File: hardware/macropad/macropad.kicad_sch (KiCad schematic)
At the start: 32 parts, among them J1 SWD, J2 USB_C_Receptacle, J4 display(4x1), SW1 SW_Push, SW10 SW_SPDT, SW11 SW_Push, SW12 Enc1, SW13 Enc2, SW2 SW_Push, SW3 SW_Push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

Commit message: updated footprints
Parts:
- C1, C3: footprint (none) -> Capacitor_SMD:C_0805_2012Metric
- C17, C18: footprint Capacitor_SMD:C_0805_2012Metric -> Capacitor_SMD:C_0603_1608Metric
- C2, C4, C5, C6, C8, C9: footprint (none) -> Capacitor_SMD:C_0603_1608Metric
- R1, R2, R4: footprint (none) -> Resistor_SMD:R_0603_1608Metric
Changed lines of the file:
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@@
 			)
 		)
-		(property "Footprint" ""
+		(property "Footprint" "Capacitor_SMD:C_0603_1608Metric"
 			(at 82.2452 46.99 0)
 			(effects
@@
 			)
 		)
-		(property "Footprint" ""
+		(property "Footprint" "Capacitor_SMD:C_0805_2012Metric"
 			(at 61.9252 46.99 0)
 			(effects
@@
 			)
 		)
-		(property "Footprint" ""
+		(property "Footprint" "Resistor_SMD:R_0603_1608Metric"
 			(at 223.012 68.58 90)
 			(effects
@@
 			)
 		)
-		(property "Footprint" ""
+		(property "Footprint" "Capacitor_SMD:C_0603_1608Metric"
 			(at 72.0852 46.99 0)
 			(effects
@@
 			)
 		)
-		(property "Footprint" "Capacitor_SMD:C_0805_2012Metric"
+		(property "Footprint" "Capacitor_SMD:C_0603_1608Metric"
 			(at 88.5952 142.24 0)
 			(effects
@@
 			)
 		)
-		(property "Footprint" ""
+		(property "Footprint" "Capacitor_SMD:C_0603_1608Metric"
 			(at 112.7252 46.99 0)
 			(effects
@@
 			)
 		)
-		(property "Footprint" ""
+		(property "Footprint" "Capacitor_SMD:C_0603_1608Metric"
 			(at 102.5652 46.99 0)
 			(effects
@@
 			)
 		)
-		(property "Footprint" "Capacitor_SMD:C_0805_2012Metric"
+		(property "Footprint" "Capacitor_SMD:C_0603_1608Metric"
 			(at 113.9952 142.24 0)
 			(effects
@@
 			)
 		)
-		(property "Footprint" ""
+		(property "Footprint" "Capacitor_SMD:C_0805_2012Metric"
 			(at 322.2752 73.66 0)
 			(effects
@@
 			)
 		)
-		(property "Footprint" ""
+		(property "Footprint" "Resistor_SMD:R_0603_1608Metric"
 			(at 391.668 156.21 90)
 			(effects
@@
 			)
 		)
-		(property "Footprint" ""
+		(property "Footprint" "Capacitor_SMD:C_0603_1608Metric"
 			(at 92.4052 46.99 0)
 			(effects
@@
 			)
 		)
-		(property "Footprint" ""
+		(property "Footprint" "Capacitor_SMD:C_0603_1608Metric"
 			(at 113.03 89.8652 0)
 			(effects
@@
 			)
 		)
-		(property "Footprint" ""
+		(property "Footprint" "Resistor_SMD:R_0603_1608Metric"
 			(at 400.558 153.67 90)
 			(effects

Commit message: updated footprints
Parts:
- SW11: footprint (none) -> Button_Switch_SMD:SW_Push_1P1T_NO_E-Switch_TL3301NxxxxxG
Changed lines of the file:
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@@
 			)
 		)
-		(property "Footprint" ""
+		(property "Footprint" "Button_Switch_SMD:SW_Push_1P1T_NO_E-Switch_TL3301NxxxxxG"
 			(at 116.84 74.93 0)
 			(effects

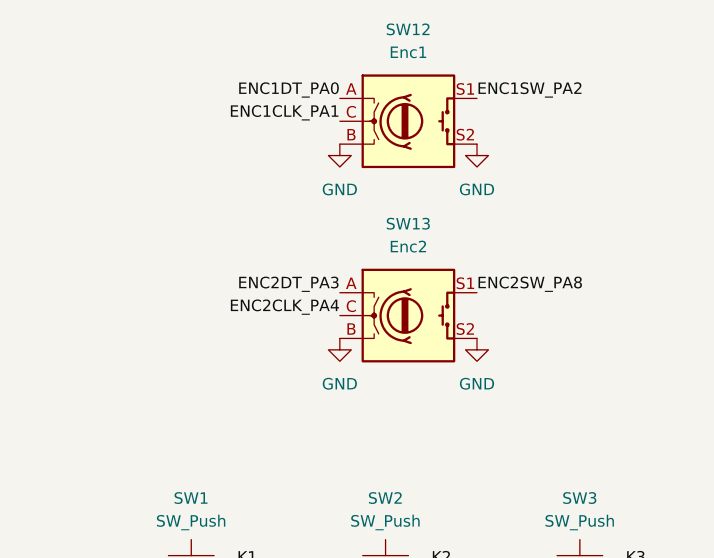
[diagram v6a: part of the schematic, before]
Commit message: replaced enc with module
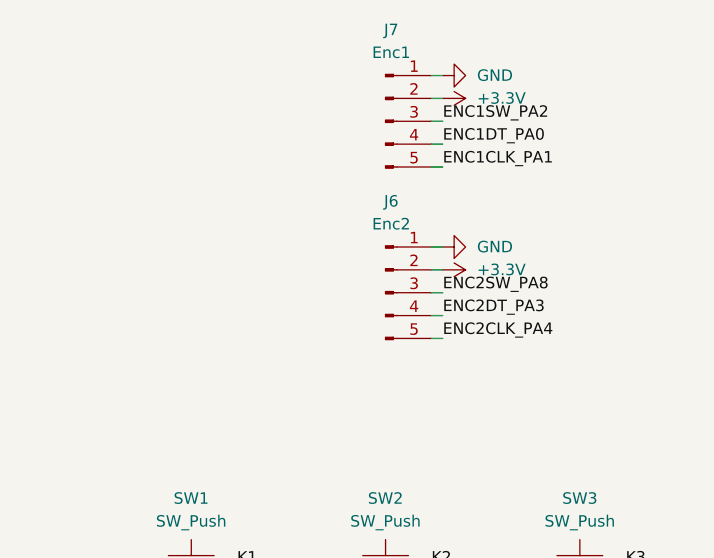
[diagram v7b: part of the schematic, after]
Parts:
- removed SW12: Enc1, symbol Device:RotaryEncoder_Switch
- removed SW13: Enc2, symbol Device:RotaryEncoder_Switch
- added J6: Enc2, Connector_PinHeader_2.54mm:PinHeader_1x05_P2.54mm_Vertical, symbol Connector:Conn_01x05_Pin
- added J7: Enc1, Connector_PinHeader_2.54mm:PinHeader_1x05_P2.54mm_Vertical, symbol Connector:Conn_01x05_Pin
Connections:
- net +3.3V: now also J6.2 (Pin_2), J7.2 (Pin_2)
- net ENC1CLK_PA1: now also J7.5 (Pin_5)
- net ENC1DT_PA0: now also J7.4 (Pin_4)
- net ENC1SW_PA2: now also J7.3 (Pin_3)
- net ENC2CLK_PA4: now also J6.5 (Pin_5)
- net ENC2DT_PA3: now also J6.4 (Pin_4)
- net ENC2SW_PA8: now also J6.3 (Pin_3)
- net GND: now also J6.1 (Pin_1), J7.1 (Pin_1)

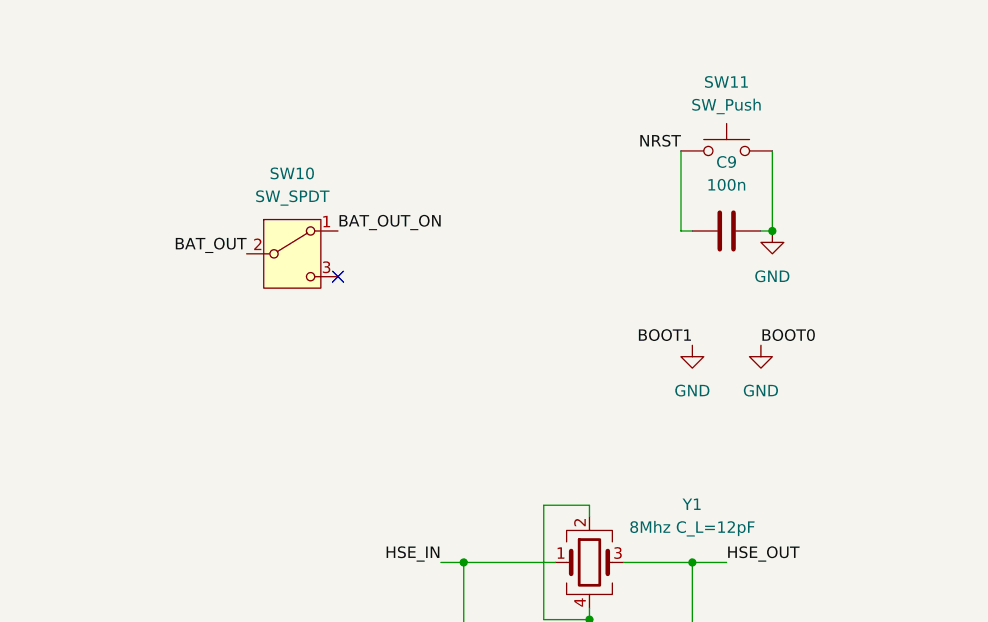
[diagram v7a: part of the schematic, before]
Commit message: updated bat switch, added 10k resistors. fixed fps
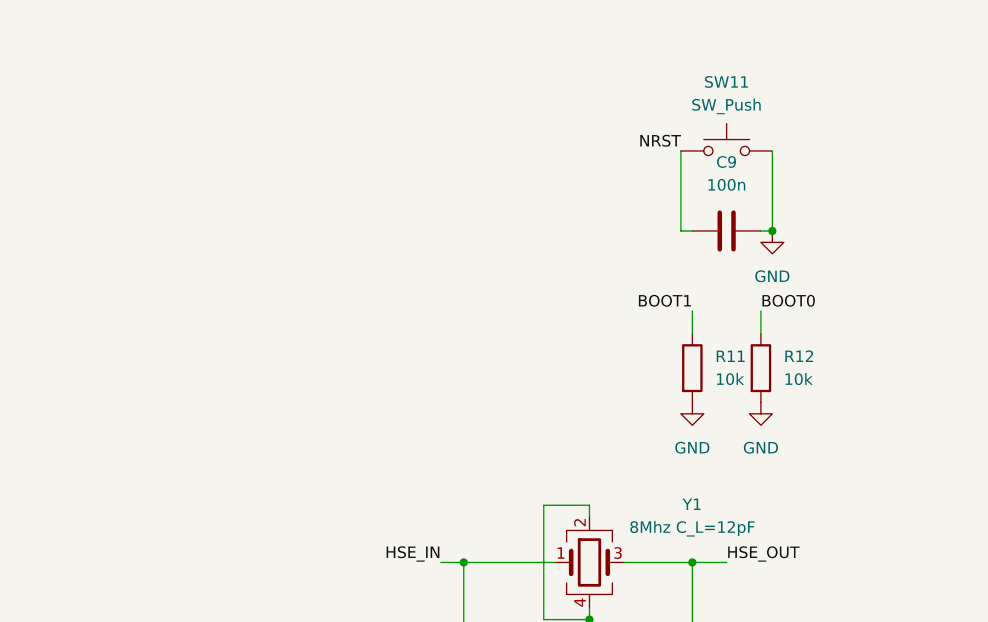
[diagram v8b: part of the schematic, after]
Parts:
- removed SW10: SW_SPDT, symbol Switch:SW_SPDT
- added R11, R12: 10k, Resistor_SMD:R_0805_2012Metric, symbol Device:R
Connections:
- net GND: now also R11.2, R12.2; no longer U2.20 (PB2), U2.44 (BOOT0)
- new net BOOT0: R12.1, U2.44 (BOOT0)
- new net BOOT1: R11.1, U2.20 (PB2)
- no-connect marks 18 -> 17
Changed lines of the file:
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@@
 	)
 	(no_connect
-		(at 73.66 93.98)
-	)
-	(no_connect
 		(at 171.45 62.23)
 	)
@@
 	(wire
 		(pts
+			(xy 113.03 100.33) (xy 113.03 97.79)
+		)
+		(stroke
+			(width 0)
+			(type default)
+		)
+	)
+	(wire
+		(pts
 			(xy 377.19 41.91) (xy 378.46 41.91)
 		)
@@
 	(wire
 		(pts
+			(xy 120.65 100.33) (xy 120.65 97.79)
+		)
+		(stroke
+			(width 0)
+			(type default)
+		)
+	)
+	(wire
+		(pts
 			(xy 101.6 142.24) (xy 113.03 142.24)
 		)
@@
 		)
 	)
-	(label "BAT_OUT_ON"
-		(at 73.66 88.9 0)
-		(effects
-			(font
-				(size 1.27 1.27)
-			)
-			(justify left bottom)
-		)
-	)
 	(label "K4"
 		(at 355.6 92.71 0)
@@
 	)
 	(label "BOOT0"
-		(at 120.65 101.6 0)
+		(at 120.65 97.79 0)
 		(effects
 			(font
@@
 	)
 	(label "BOOT1"
-		(at 113.03 101.6 180)
+		(at 113.03 97.79 180)
 		(effects
 			(font
@@
 		)
 	)
-	(label "BAT_OUT"
-		(at 63.5 91.44 180)
-		(effects
-			(font
-				(size 1.27 1.27)
-			)
-			(justify right bottom)
-		)
-	)
 	(label "PB0"
 		(at 269.24 68.58 0)
@@
 	)
 	(symbol
+		(lib_id "Device:R")
+		(at 113.03 104.14 0)
+		(unit 1)
+		(exclude_from_sim no)
+		(in_bom yes)
+		(on_board yes)
+		(dnp no)
+		(fields_autoplaced yes)
+		(property "Reference" "R11"
+			(at 115.57 102.8699 0)
+			(effects
+				(font
+					(size 1.27 1.27)
+				)
+				(justify left)
+			)
+		)
+		(property "Value" "10k"
+			(at 115.57 105.4099 0)
+			(effects
+				(font
+					(size 1.27 1.27)
+				)
+				(justify left)
+			)
+		)
+		(property "Footprint" "Resistor_SMD:R_0805_2012Metric"
+			(at 111.252 104.14 90)
+			(effects
+				(font
+					(size 1.27 1.27)
+				)
+				(hide yes)
+			)
+		)
+		(property "Datasheet" "~"
+			(at 113.03 104.14 0)
+			(effects
+				(font
+					(size 1.27 1.27)
+				)
+				(hide yes)
+			)
+		)
+		(property "Description" "Resistor"
+			(at 113.03 104.14 0)
+			(effects
+				(font
+					(size 1.27 1.27)
+				)
+				(hide yes)
+			)
+		)
+		(pin "1"
+		)
+		(pin "2"
+		)
+		(instances
+			(project ""
+				(path "/228dc472-b306-4e5f-8dc5-2bf23eb4978d"
+					(reference "R11")
+					(unit 1)
+				)
+			)
+		)
+	)
+	(symbol
 		(lib_id "power:GND")
 		(at 121.92 88.9 0)
@@
 	)
 	(symbol
-		(lib_id "Switch:SW_SPDT")
-		(at 68.58 91.44 0)
+		(lib_id "Device:R")
+		(at 120.65 104.14 0)
 		(unit 1)
 		(exclude_from_sim no)
@@
 		(dnp no)
 		(fields_autoplaced yes)
-		(property "Reference" "SW10"
-			(at 68.58 82.55 0)
+		(property "Reference" "R12"
+			(at 123.19 102.8699 0)
 			(effects
 				(font
 					(size 1.27 1.27)
 				)
+				(justify left)
 			)
 		)
-		(property "Value" "SW_SPDT"
-			(at 68.58 85.09 0)
+		(property "Value" "10k"
+			(at 123.19 105.4099 0)
 			(effects
 				(font
 					(size 1.27 1.27)
 				)
+				(justify left)
 			)
 		)
-		(property "Footprint" ""
-			(at 68.58 91.44 0)
+		(property "Footprint" "Resistor_SMD:R_0805_2012Metric"
+			(at 118.872 104.14 90)
 			(effects
 				(font
@@
 		)
 		(property "Datasheet" "~"
-			(at 68.58 99.06 0)
+			(at 120.65 104.14 0)
 			(effects
 				(font
@@
 			)
 		)
-		(property "Description" "Switch, single pole double throw"
-			(at 68.58 91.44 0)
+		(property "Description" "Resistor"
+			(at 120.65 104.14 0)
 			(effects
 				(font
@@
 			)
 		)
-		(pin "3"
+		(pin "1"
 		)
 		(pin "2"
 		)
-		(pin "1"
-		)
 		(instances
-			(project ""
+			(project "macropad"
 				(path "/228dc472-b306-4e5f-8dc5-2bf23eb4978d"
-					(reference "SW10")
+					(reference "R12")
 					(unit 1)
 				)
@@
 	(symbol
 		(lib_id "power:GND")
-		(at 120.65 101.6 0)
+		(at 120.65 107.95 0)
 		(unit 1)
 		(exclude_from_sim no)
@@
 		(fields_autoplaced yes)
 		(property "Reference" "#PWR025"
-			(at 120.65 107.95 0)
+			(at 120.65 114.3 0)
 			(effects
 				(font
@@
 		)
 		(property "Value" "GND"
-			(at 120.65 106.68 0)
+			(at 120.65 113.03 0)
 			(effects
 				(font
@@
 		)
 		(property "Footprint" ""
-			(at 120.65 101.6 0)
+			(at 120.65 107.95 0)
 			(effects
 				(font
@@
 		)
 		(property "Datasheet" ""
-			(at 120.65 101.6 0)
+			(at 120.65 107.95 0)
 			(effects
 				(font
@@
 		)
 		(property "Description" "Power symbol creates a global label with name \"GND\" , ground"
-			(at 120.65 101.6 0)
+			(at 120.65 107.95 0)
 			(effects
 				(font
@@
 	(symbol
 		(lib_id "power:GND")
-		(at 113.03 101.6 0)
+		(at 113.03 107.95 0)
 		(unit 1)
 		(exclude_from_sim no)
@@
 		(fields_autoplaced yes)
 		(property "Reference" "#PWR010"
-			(at 113.03 107.95 0)
+			(at 113.03 114.3 0)
 			(effects
 				(font
@@
 		)
 		(property "Value" "GND"
-			(at 113.03 106.68 0)
+			(at 113.03 113.03 0)
 			(effects
 				(font
@@
 		)
 		(property "Footprint" ""
-			(at 113.03 101.6 0)
+			(at 113.03 107.95 0)
 			(effects
 				(font
@@
 		)
 		(property "Datasheet" ""
-			(at 113.03 101.6 0)
+			(at 113.03 107.95 0)
 			(effects
 				(font
@@
 		)
 		(property "Description" "Power symbol creates a global label with name \"GND\" , ground"
-			(at 113.03 101.6 0)
+			(at 113.03 107.95 0)
 			(effects
 				(font
